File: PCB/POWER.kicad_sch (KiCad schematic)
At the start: 9 parts, among them U1 LSM303AH, U2 TCA39306DCUR

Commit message: WIP
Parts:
- removed C12, C7: C_100nF_50V_10%_X7R_0402_H0.55, 002-Capacitors:C_0402_H0.55, symbol 002-Capacitors:C_100nF_50V_10%_X7R_0402
- removed C13: C_220nF_50V_10%_X7R_0603_H0.9, 002-Capacitors:C_0603_H0.95, symbol 002-Capacitors:C_220nF_50V_10%_X7R_0603
- removed C14: C_10uF_10V_20%_X5R_0603H0.9, 002-Capacitors:C_0603_H0.95, symbol 002-Capacitors:C_10uF_10V_20%_X5R_0603
- removed R5, R7: R_4k7_1%_1/10W_0603, 001-Resistors:R_0603_H0.55, symbol 001-Resistors:R_4k7_1%_1/10W_0603
- removed R8: R_200k_1%_1/16W_0402, 001-Resistors:R_0402_H0.4, symbol Resistors:R_200k_1%_1/16W_0402
- removed U1: LSM303AH, 008-Sensors:LSM303AHTR, symbol 008-Sensors:LSM303AHTR
- removed U2: TCA39306DCUR, 005-ICs:TCA39306DCUR, symbol ICs:TCA39306DCUR
- added C10, C11, C8: C_1uF_50V_10%_X5R_0603_H0.9, 002-Capacitors:C_0603_H0.95, symbol 002-Capacitors:C_1uF_50V_10%_X5R_0603
- added C15: C_4.7uF_10V_10%_X7S_0603_H0.95, 002-Capacitors:C_0603_H0.95, symbol 002-Capacitors:C_4.7uF_10V_10%_X7S_0603
- added C9: C_100nF_50V_10%_X7R_0402_H0.55, 002-Capacitors:C_0402_H0.55, symbol 002-Capacitors:C_100nF_50V_10%_X7R_0402
- added IC1: MIC5330-SSYML-TR, 004-Power:MIC5330, symbol 004-Power:MIC5330-SSYML-TR
- added U7: AAA_2X_Holder, 004-Power:AAA_2X_Holder, symbol 004-Power:AAA_2X_Holder
- added U8: TPS610333DRLR, 004-Power:TPS610333DRLR, symbol 004-Power:TPS610333DRLR
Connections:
- net +3.3V: now also C10.1, IC1.8 (VOUT1)
- net GND: now also C10.2, C11.2, C15.2, C8.2, C9.2, IC1.2 (GND), IC1.9 (PAD), U7.2, U8.3 (MODE), U8.6 (GND)
- new net: C9.1, IC1.3 (BYP)
- new net: U8.1 (VIN), U8.2 (EN), U8.5 (FB)
- new net +3.3V_RYLR: C11.1, IC1.7 (VOUT2)
- new net +5V: C8.1, IC1.1 (VIN), IC1.5 (EN1), U8.8 (VOUT)
- new net +VBAT: C15.1, U7.1
- new net RYLR_3V3_EN: IC1.4 (EN2)
- no-connect marks 0 -> 1
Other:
- note added: "Switch + capacitor"
- note added: "capacitor"
- note removed: "Magnetometer + accelerometer"
- note removed: "acc: 0x1D (?) mag: 0x1E (?)"

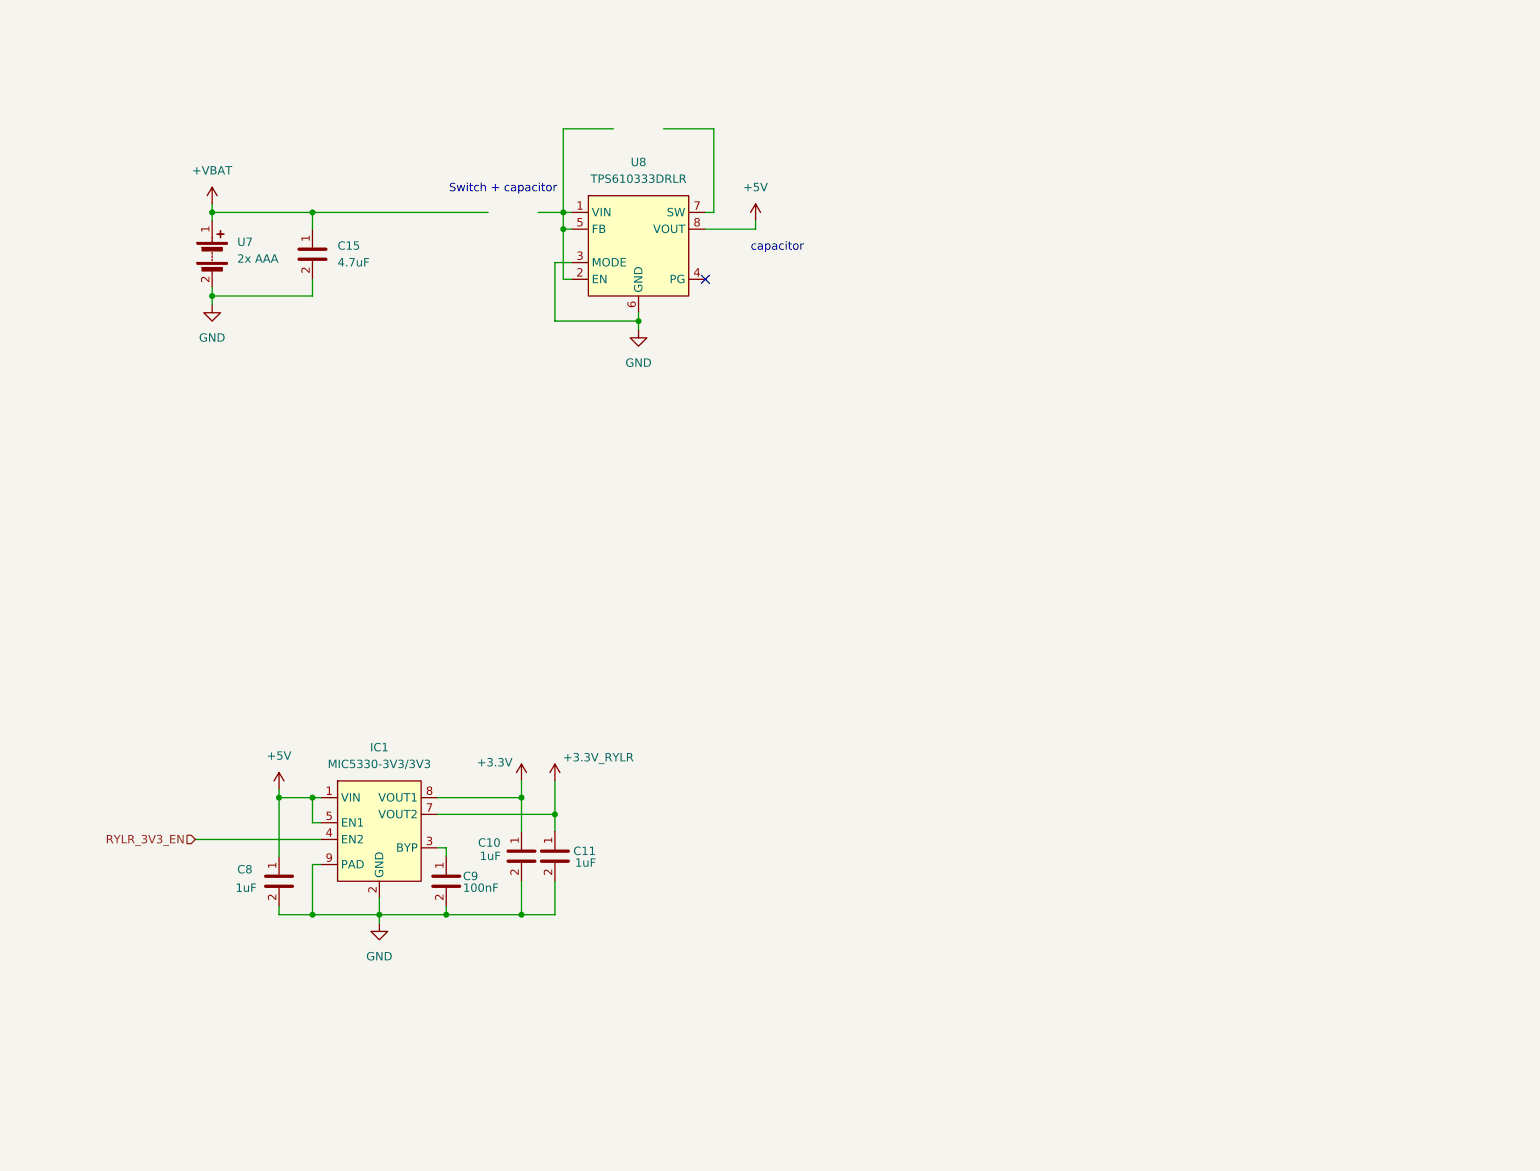
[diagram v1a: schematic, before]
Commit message: Add LEDs
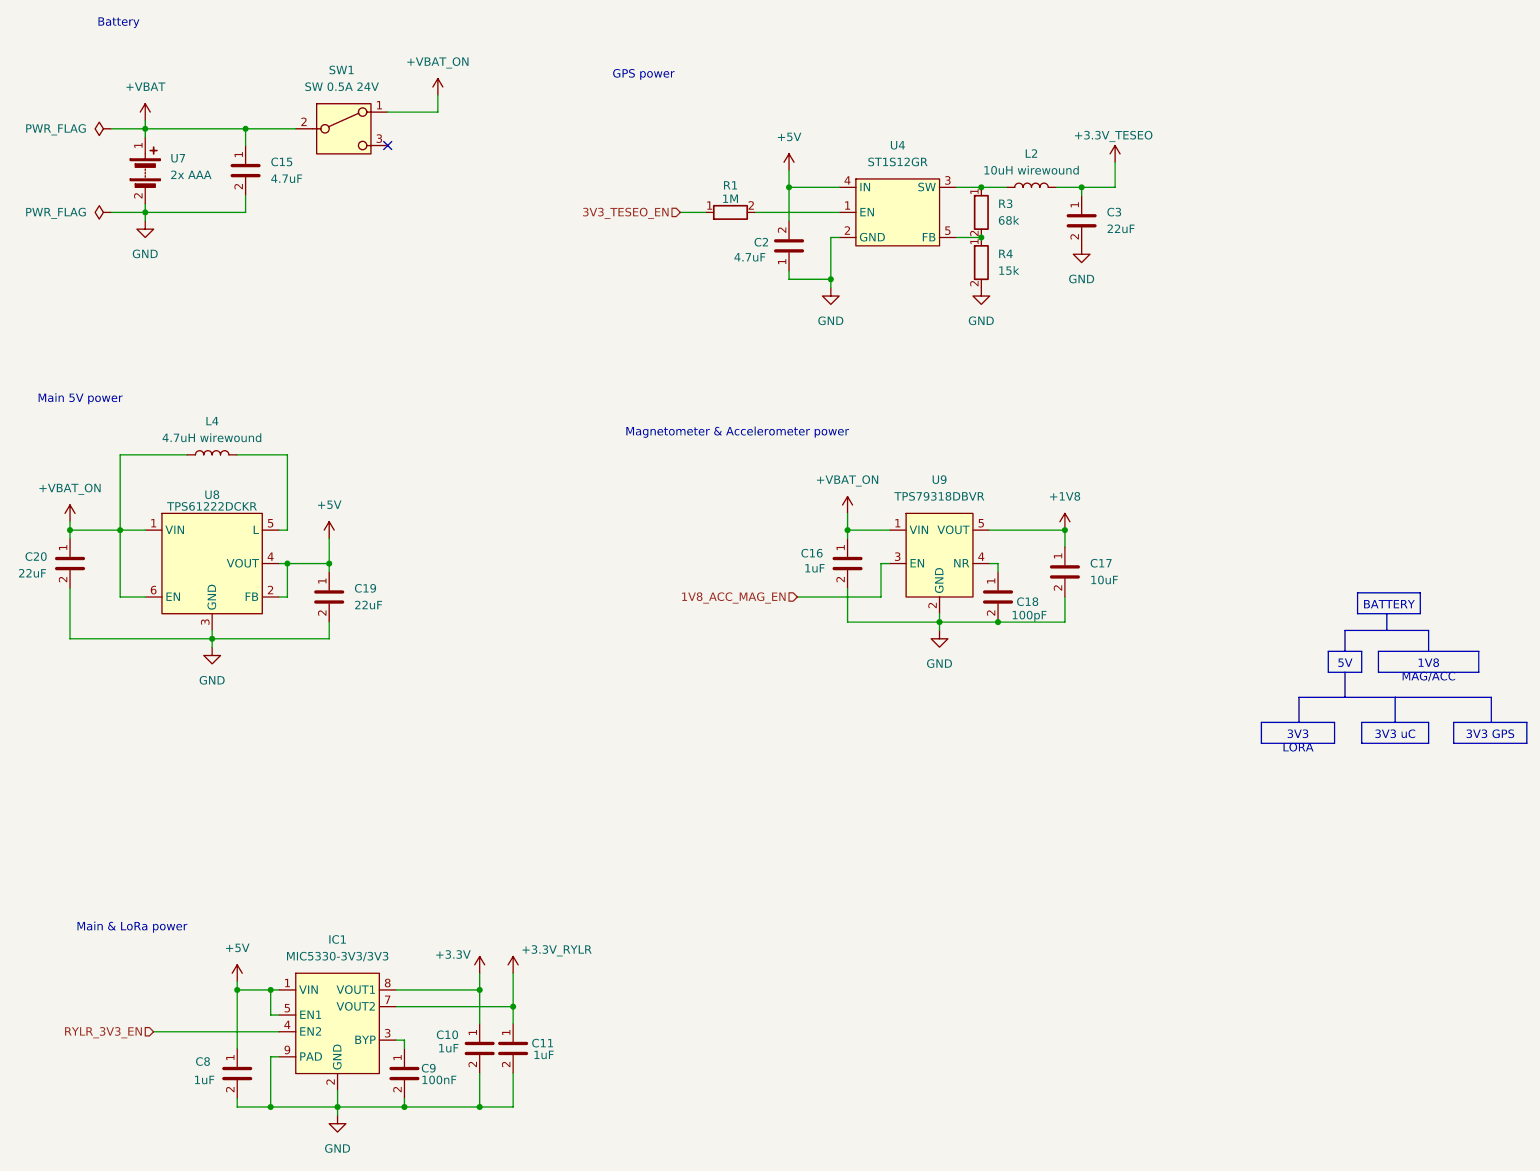
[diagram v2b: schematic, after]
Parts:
- removed U8: TPS610333DRLR, 004-Power:TPS610333DRLR, symbol 004-Power:TPS610333DRLR
- added C16: C_1uF_50V_10%_X5R_0603_H0.9, 002-Capacitors:C_0603_H0.95, symbol 002-Capacitors:C_1uF_50V_10%_X5R_0603
- added C17: C_10uF_10V_20%_X5R_0603H0.9, 002-Capacitors:C_0603_H0.95, symbol 002-Capacitors:C_10uF_10V_20%_X5R_0603
- added C18: C_100pF_50V_5%_C0G_0603_H0.9, 002-Capacitors:C_0603_H0.95, symbol 002-Capacitors:GRM1885C1H101JA01D
- added C19, C20: C_22uF_25V_20%_X5S_0603_H1, 002-Capacitors:C_0603_H0.95, symbol 002-Capacitors:C_22uF_25V_20%_X5S_0603
- added C2: C_4.7uF_10V_10%_X7S_0603_H0.95, 002-Capacitors:C_0603_H0.95, symbol 002-Capacitors:C_4.7uF_10V_10%_X7S_0603
- added C3: C_22uF_6.3V_20%_X5R_0805_H1.4, 002-Capacitors:C_0805_H1.4, symbol 002-Capacitors:C_22uF_6.3V_20%_X5R_0805
- added L2: L_10uH_20%_1.51A_160mOhm, 003-Inductors:LTF5022T-100M1R3-D, symbol 003-Inductors:L_10uH_20%_1.51A_160mOhm
- added L4: L_4.7uH_20%_850mA_168mOhm, 003-Inductors:LQH3NPZ4R7MGRL, symbol 003-Inductors:L_4.7uH_20%_850mA_168mOhm
- added R1: R_1M_5%_1/16W_0402, 001-Resistors:R_0402_H0.4, symbol 001-Resistors:R_1M_5%_1/16W_0402
- added R3: R_68k_1%_1/16W_0402, 001-Resistors:R_0402_H0.4, symbol 001-Resistors:R_68k_1%_1/16W_0402
- added R4: R_15k_1%_1/16W_0402, 001-Resistors:R_0402_H0.4, symbol 001-Resistors:R_15k_1%_1/16W_0402
- added SW1: switch_slide_2pos, 009-Connectors:09.10290.01, symbol 009-Connectors:switch_slide_2pos
- added U4: ST1S12GR, 004-Power:ST1S12GR, symbol 004-Power:ST1S12GR
- added U8: TPS61222DCKR, 004-Power:TPS61222DCKR, symbol 004-Power:TPS61222DCKR
- added U9: TPS79318DBVR, 004-Power:TPS79318DBVR, symbol 004-Power:TPS79318DBVR
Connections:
- net +5V: now also C19.1, C2.2, U4.4 (IN), U8.2 (FB), U8.4 (VOUT)
- net +VBAT: now also SW1.2
- net GND: now also C16.2, C17.2, C18.2, C19.2, C2.1, C20.2, C3.2, R4.2, U4.2 (GND), U8.3 (GND), U9.2 (GND)
- new net: L2.1, R3.1, U4.3 (SW)
- new net: R1.2, U4.1 (EN)
- new net: L4.2, U8.5 (L)
- new net: R3.2, R4.1, U4.5 (FB)
- new net: C18.1, U9.4 (NR)
- new net +1V8: C17.1, U9.5 (VOUT)
- new net +3.3V_TESEO: C3.1, L2.2
- new net +VBAT_ON: C16.1, C20.1, L4.1, SW1.1, U8.1 (VIN), U8.6 (EN), U9.1 (VIN)
- new net 1V8_ACC_MAG_EN: U9.3 (EN)
- new net 3V3_TESEO_EN: R1.1
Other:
- note added: "Battery"
- note added: "GPS power"
- note added: "Magnetometer & Accelerometer power"
- note added: "Main & LoRa power"
- note added: "Main 5V power"
- note removed: "Switch + capacitor"
- note removed: "capacitor"
- moved on the sheet: C10, C11, C15, C8, C9, U7

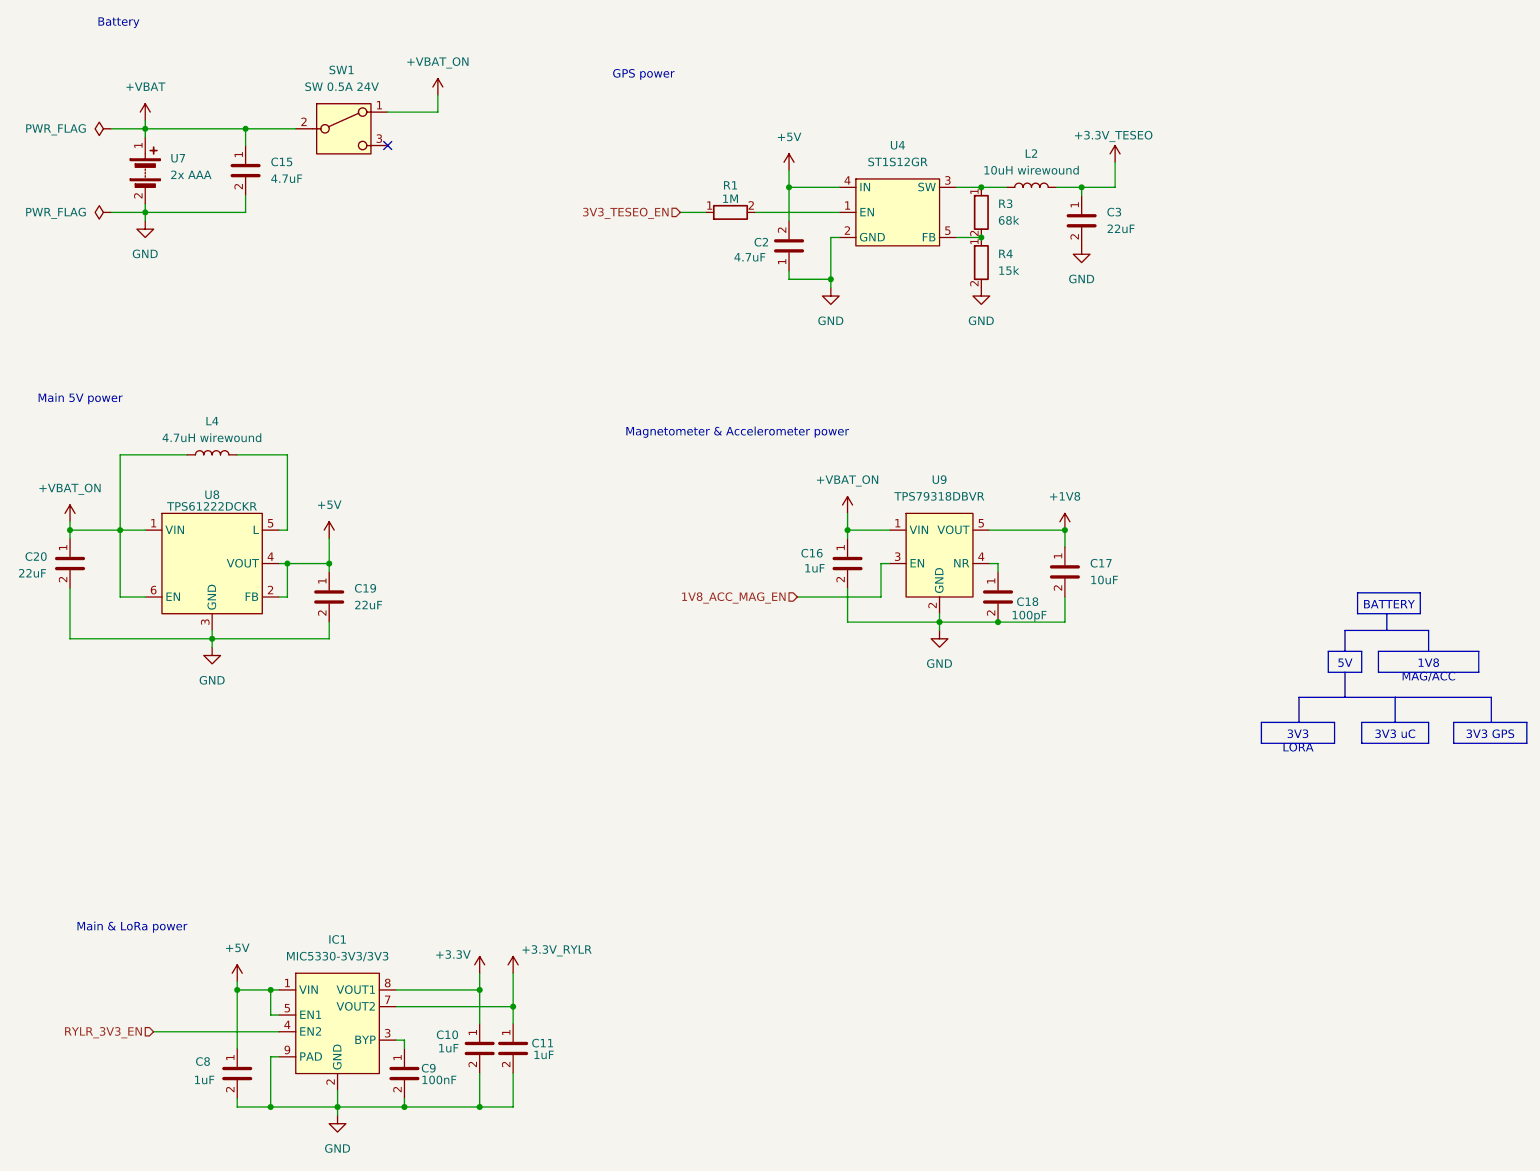
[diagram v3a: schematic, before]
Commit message: Finish schematic minus mcu
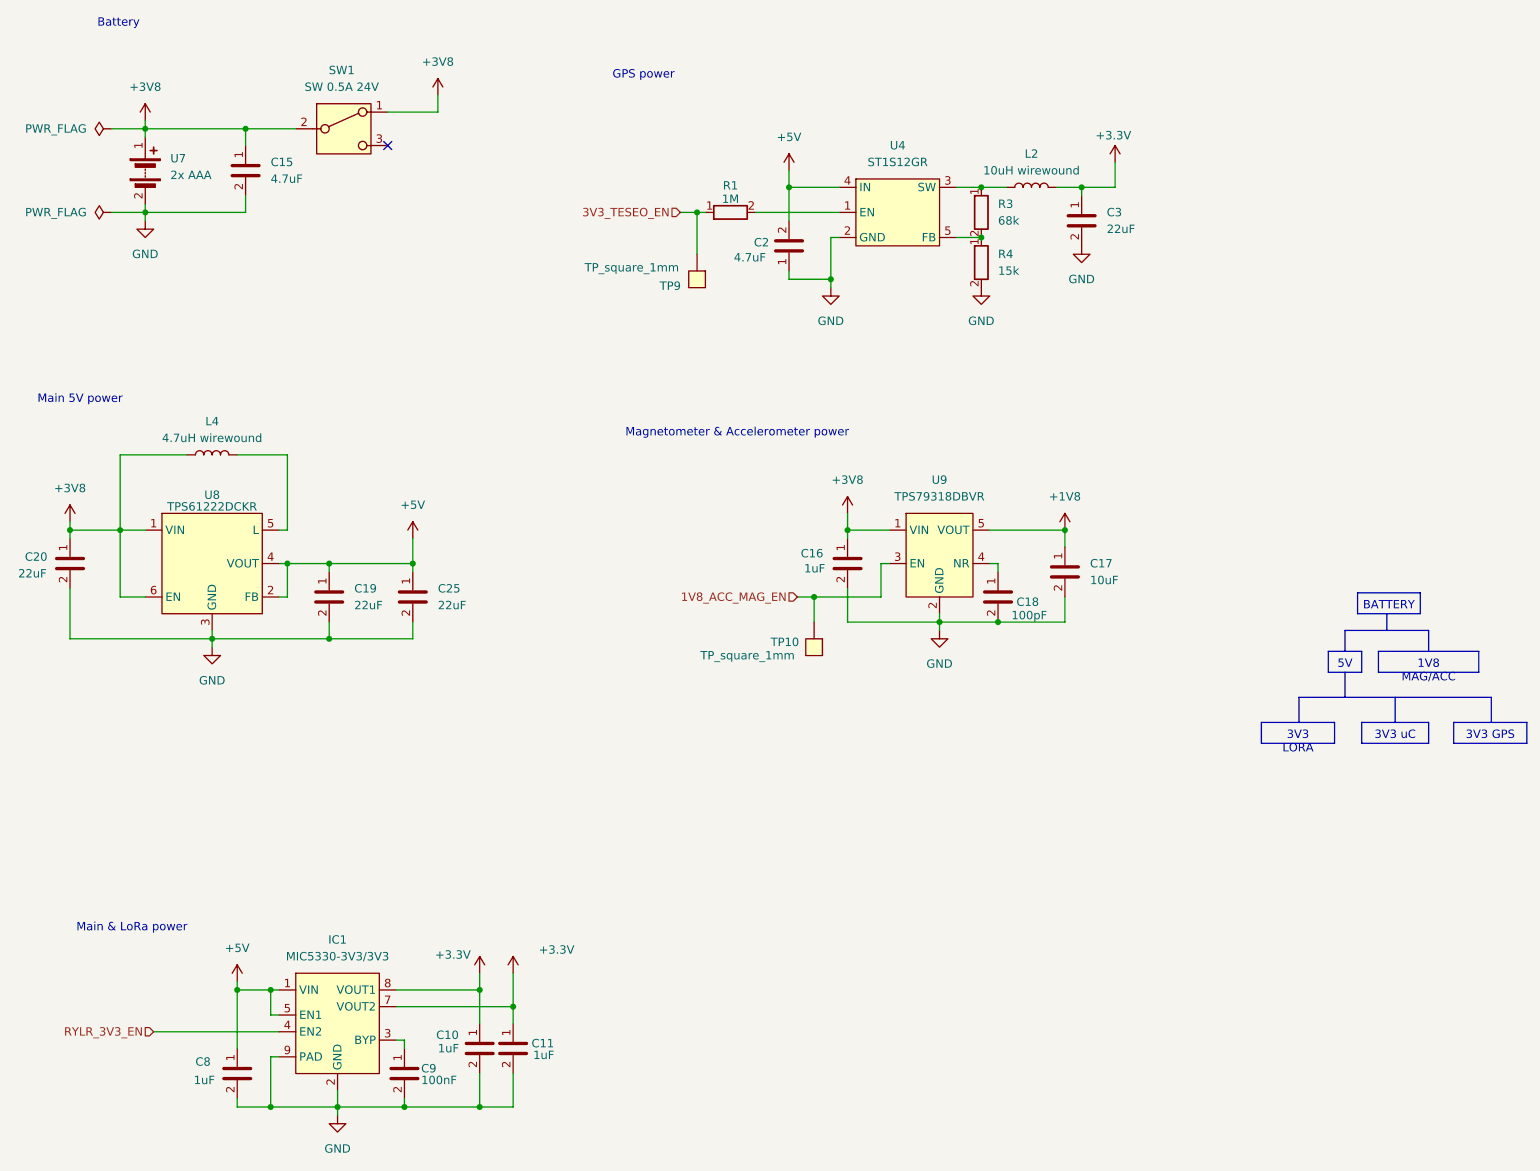
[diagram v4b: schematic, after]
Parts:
- added C25: C_22uF_25V_20%_X5S_0603_H1, 002-Capacitors:C_0603_H0.95, symbol 002-Capacitors:C_22uF_25V_20%_X5S_0603
- added TP10, TP9: TP_square_1mm, 011-Misc:Testpoint_square_1mm, symbol 011-Misc:Testpoint_square_1mm
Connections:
- net +3.3V_RYLR is gone; now on net +3.3V: C11.1, IC1.7 (VOUT2)
- net +3.3V_TESEO is gone; now on net +3.3V: C3.1, L2.2
- net +VBAT_ON is gone; now on net +3V8: C16.1, C20.1, L4.1, SW1.1, U8.1 (VIN), U8.6 (EN), U9.1 (VIN)
- net +5V: now also C25.1
- net 1V8_ACC_MAG_EN: now also TP10.
- net 3V3_TESEO_EN: now also TP9.
- net GND: now also C25.2
- net +VBAT renamed +3V8

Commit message: Layout start
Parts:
- removed C10, C11, C8: C_1uF_50V_10%_X5R_0603_H0.9, 002-Capacitors:C_0603_H0.95, symbol 002-Capacitors:C_1uF_50V_10%_X5R_0603
- removed C17: C_10uF_10V_20%_X5R_0603H0.9, 002-Capacitors:C_0603_H0.95, symbol 002-Capacitors:C_10uF_10V_20%_X5R_0603
- removed IC1: MIC5330-SSYML-TR, 004-Power:MIC5330, symbol 004-Power:MIC5330-SSYML-TR
- removed TP10, TP9: TP_square_1mm, 011-Misc:Testpoint_square_1mm, symbol 011-Misc:Testpoint_square_1mm
- added C10, C11, C8: C_1uF_50V_10%_X5R_0402_H0.55, 002-Capacitors:C_0402_H0.55, symbol 002-Capacitors:C_1uF_50V_10%_X5R_0402
- added C13: C_2.2uF_25V_25%_X5R_0402_H0.55, 002-Capacitors:C_0402_H0.55, symbol 002-Capacitors:C_2.2uF_25V_25%_X5R_0402
- added U13: MIC5330-SSYML-TR, 004-Power:MIC5330, symbol 004-Power:MIC5330-SSYML-TR
- renumbered U7 to B7
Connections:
- net +1V8: now also C13.1
- net +3.3V: now also C10.1, U13.8 (VOUT1); no longer C3.1, L2.2
- net +5V: now also C8.1, U13.1 (VIN), U13.5 (EN1)
- net GND: now also C10.2, C11.2, C13.2, C8.2, U13.2 (GND), U13.9 (PAD)
- net RYLR_3V3_EN: now also U13.4 (EN2)
- net +3V0: now reaches SW1.3
- net +3V0: now also C16.1, C20.1, L4.1, U8.1 (VIN), U8.6 (EN), U9.1 (VIN)
- net at C9.1: now also U13.3 (BYP)
- removed net +3V8: B7.1, C15.1, C16.1, C20.1, L4.1, SW1.1, SW1.2, U8.1 (VIN), U8.6 (EN), U9.1 (VIN)
- new net +3.3V_GPS: C3.1, L2.2
- new net +3.3V_LORA: C11.1, U13.7 (VOUT2)
- new net +BATT: B7.1, C15.1, SW1.2

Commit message: First layout draft
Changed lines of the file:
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@@
+	)
+	(junction
+		(at 186.69 44.45)
+		(diameter 0)
+		(color 0 0 0 0)
 	)
 	(junction
@@
 					(unit 1)
 				)
+			)
+		)
+	)
+	(symbol
+		(lib_id "power:PWR_FLAG")
+		(at 186.69 44.45 270)
+		(unit 1)
+		(exclude_from_sim no)
+		(in_bom yes)
+		(on_board yes)
+		(dnp no)
+		(fields_autoplaced yes)
+		(property "Reference" "#FLG04"
+			(at 188.595 44.45 0)
+			(effects
+				(font
+					(size 1.27 1.27)
+				)
+				(hide yes)
+			)
+		)
+		(property "Value" "PWR_FLAG"
+			(at 190.5 44.4499 90)
+			(effects
+				(font
+					(size 1.27 1.27)
+				)
+				(justify left)
+			)
+		)
+		(property "Footprint" ""
+			(at 186.69 44.45 0)
+			(effects
+				(font
+					(size 1.27 1.27)
+				)
+				(hide yes)
+			)
+		)
+		(property "Datasheet" "~"
+			(at 186.69 44.45 0)
+			(effects
+				(font
+					(size 1.27 1.27)
+				)
+				(hide yes)
+			)
+		)
+		(property "Description" "Special symbol for telling ERC where power comes from"
+			(at 186.69 44.45 0)
+			(effects
+				(font
+					(size 1.27 1.27)
+				)
+				(hide yes)
+			)
+		)
+		(pin "1"
+		)
+		(instances
+			(project "relativeGPS"
+				(path "/9255e348-2f0c-48d3-8a71-46491dcb1a12/15c1922d-035b-4771-885b-611376c0a6b7"
+					(reference "#FLG04")
+					(unit 1)
+				)

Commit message: Add TPs
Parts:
- added TP1, TP11, TP2, TP3, TP4, TP5, TP6, TP7: TP_square_1mm, 011-Misc:Testpoint_square_1mm, symbol 011-Misc:Testpoint_square_1mm
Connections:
- net +1V8: now also TP7.1
- net +3.3V: now also TP6.1
- net +3.3V_GPS: now also TP4.1
- net +3.3V_LORA: now also TP5.1
- net +3V0: now also TP2.1
- net +5V: now also TP3.1
- net +BATT: now also TP1.1
- net GND: now also TP11.1
